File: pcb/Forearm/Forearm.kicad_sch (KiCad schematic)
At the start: 9 parts, among them J1 Conn_01x08_IMU_0, J2 Conn_01x16_Ribbon_To_Top, J3 Conn_01x16_Ribbon_To_Bottom, J4 Conn_01x03_DFR0205, U1 ESP32-S3-DEVKITC-1-N8R2

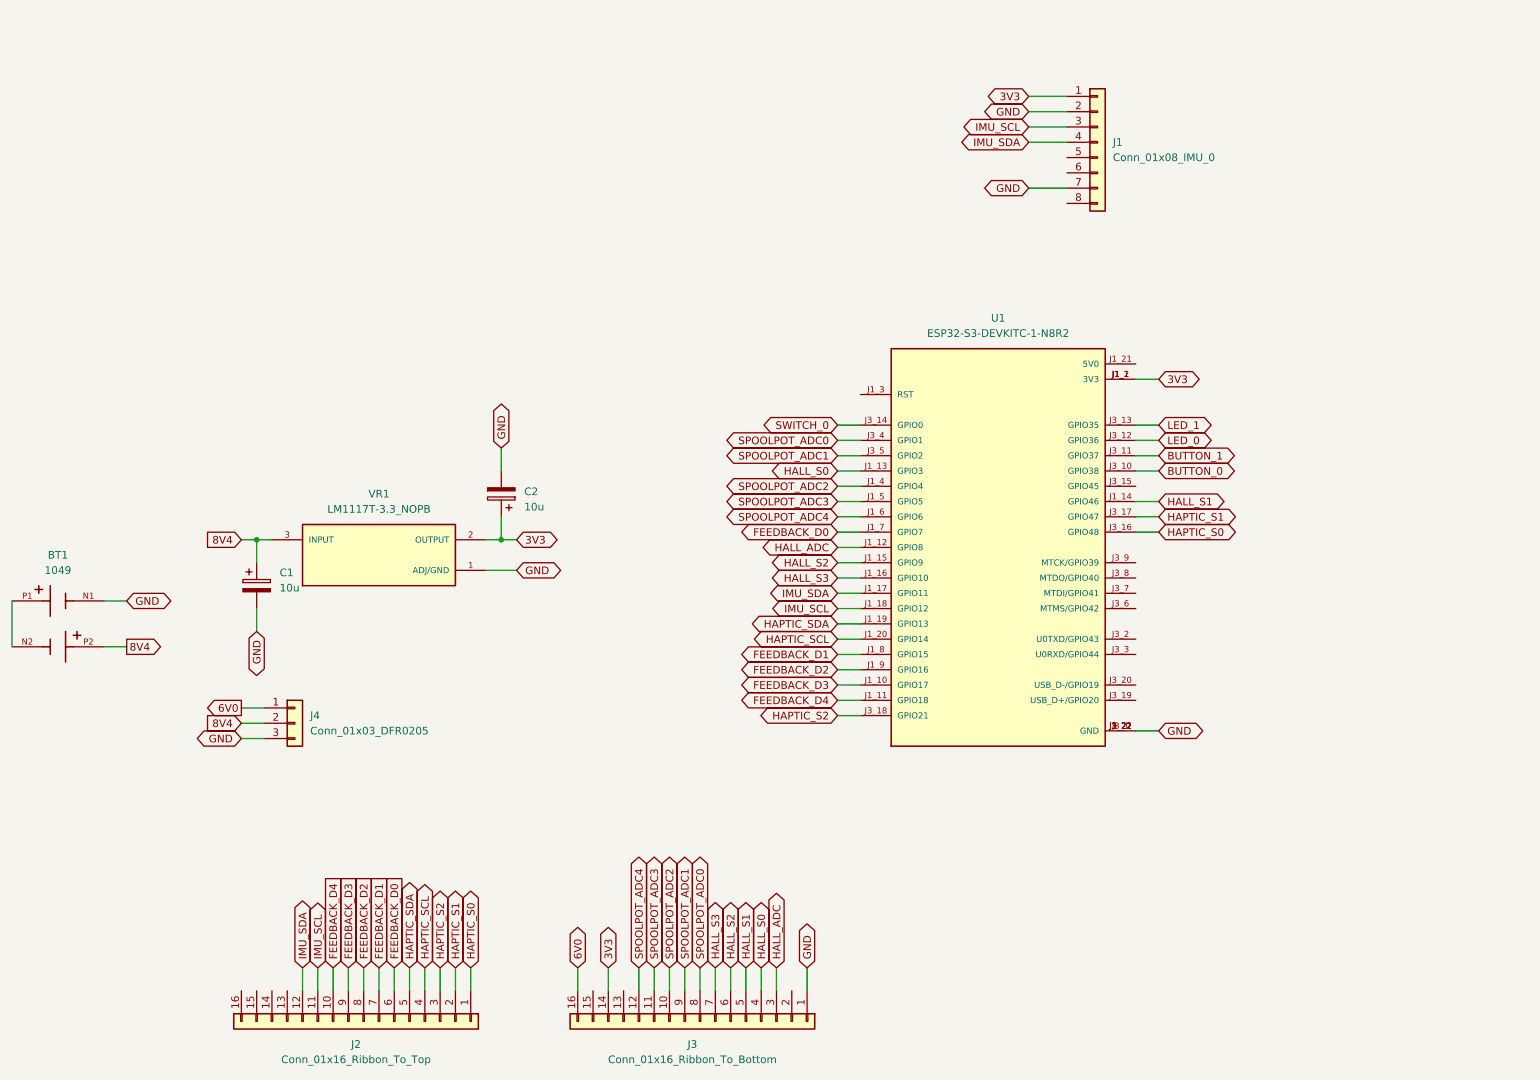
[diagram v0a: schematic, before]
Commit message: merging jackson pcb into main
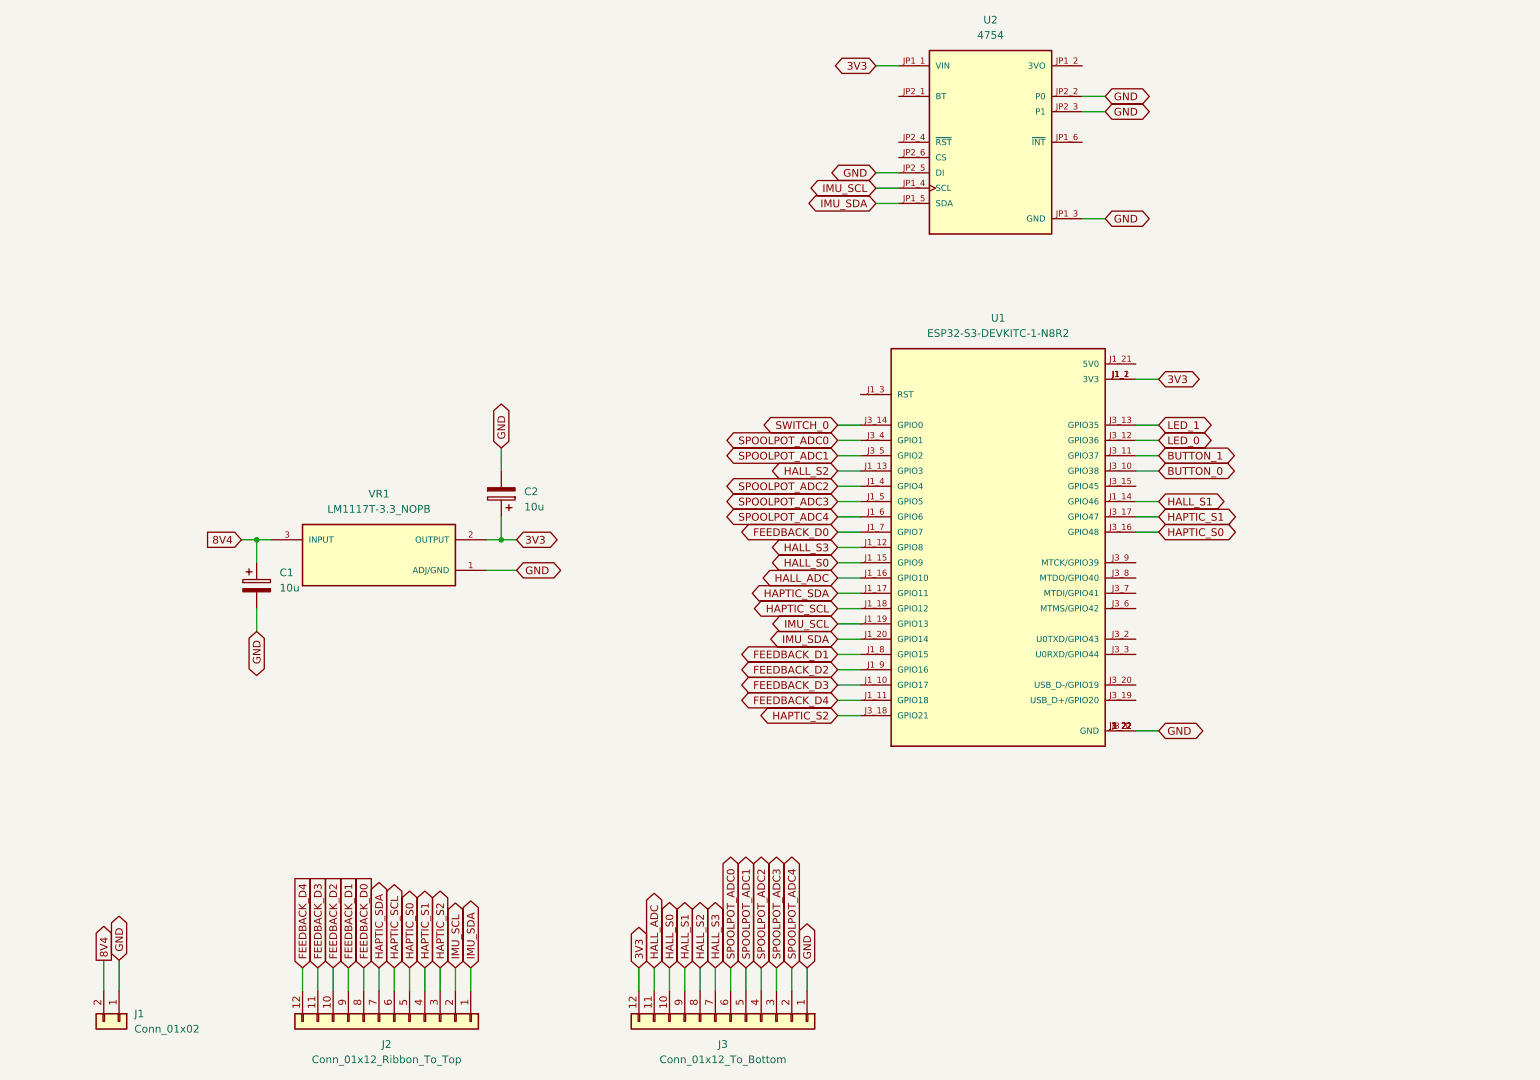
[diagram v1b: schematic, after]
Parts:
- removed BT1: 1049, 1049:BAT_1049, symbol 1049:1049
- removed J1: Conn_01x08_IMU_0, symbol Connector_Generic:Conn_01x08
- removed J2: Conn_01x16_Ribbon_To_Top, symbol Connector_Generic:Conn_01x16
- removed J3: Conn_01x16_Ribbon_To_Bottom, symbol Connector_Generic:Conn_01x16
- removed J4: Conn_01x03_DFR0205, symbol Connector_Generic:Conn_01x03
- added J1: Conn_01x02, Connector_PinSocket_2.54mm:PinSocket_1x02_P2.54mm_Vertical, symbol Connector_Generic:Conn_01x02
- added J2: Conn_01x12_Ribbon_To_Top, 0522071233:0522071233, symbol Connector_Generic:Conn_01x12
- added J3: Conn_01x12_To_Bottom, 0522071233:0522071233, symbol Connector_Generic:Conn_01x12
- added U2: 4754, BNO085:MODULE_4754, symbol BNO085:4754
- C1, C2: footprint (none) -> Capacitor_SMD:C_1206_3216Metric
- VR1: footprint LM1117T-3.3_NOPB:TO254P1054X470X1955-3 -> LM1117T-3.3:LM1117T-3.3_NOPB
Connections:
- net 3V3: now also J3.12 (Pin_12), U2.JP1_1 (VIN)
- net 8V4: now also J1.2 (Pin_2)
- net FEEDBACK_D0: now also J2.8 (Pin_8)
- net FEEDBACK_D1: now also J2.9 (Pin_9)
- net FEEDBACK_D2: now also J2.10 (Pin_10)
- net FEEDBACK_D3: now also J2.11 (Pin_11)
- net FEEDBACK_D4: now also J2.12 (Pin_12)
- net GND: now also J1.1 (Pin_1), J3.1 (Pin_1), U2.JP1_3 (GND), U2.JP2_2 (P0), U2.JP2_3 (P1), U2.JP2_5 (DI)
- net HALL_ADC: now also U1.J1_16 (GPIO10), J3.11 (Pin_11); no longer U1.J1_12 (GPIO8)
- net HALL_S0: now also U1.J1_15 (GPIO9), J3.10 (Pin_10); no longer U1.J1_13 (GPIO3)
- net HALL_S1: now also J3.9 (Pin_9)
- net HALL_S2: now also U1.J1_13 (GPIO3), J3.8 (Pin_8); no longer U1.J1_15 (GPIO9)
- net HALL_S3: now also U1.J1_12 (GPIO8), J3.7 (Pin_7); no longer U1.J1_16 (GPIO10)
- net HAPTIC_S0: now also J2.5 (Pin_5)
- net HAPTIC_S1: now also J2.4 (Pin_4)
- net HAPTIC_S2: now also J2.3 (Pin_3)
- net HAPTIC_SCL: now also U1.J1_18 (GPIO12), J2.6 (Pin_6); no longer U1.J1_20 (GPIO14)
- net HAPTIC_SDA: now also U1.J1_17 (GPIO11), J2.7 (Pin_7); no longer U1.J1_19 (GPIO13)
- net IMU_SCL: now also U1.J1_19 (GPIO13), J2.2 (Pin_2), U2.JP1_4 (SCL); no longer U1.J1_18 (GPIO12)
- net IMU_SDA: now also U1.J1_20 (GPIO14), J2.1 (Pin_1), U2.JP1_5 (SDA); no longer U1.J1_17 (GPIO11)
- net SPOOLPOT_ADC0: now also J3.6 (Pin_6)
- net SPOOLPOT_ADC1: now also J3.5 (Pin_5)
- net SPOOLPOT_ADC2: now also J3.4 (Pin_4)
- net SPOOLPOT_ADC3: now also J3.3 (Pin_3)
- net SPOOLPOT_ADC4: now also J3.2 (Pin_2)

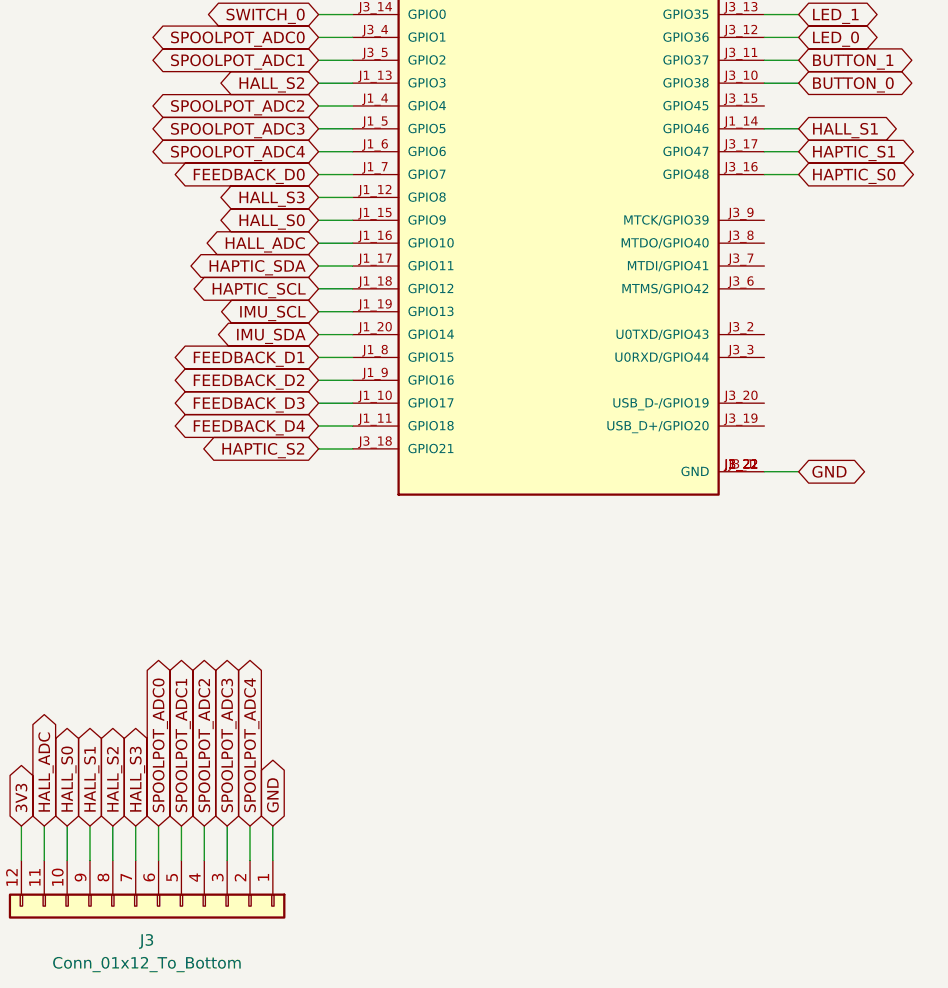
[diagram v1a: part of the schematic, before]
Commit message: re-routed forearm board w/o switches etc
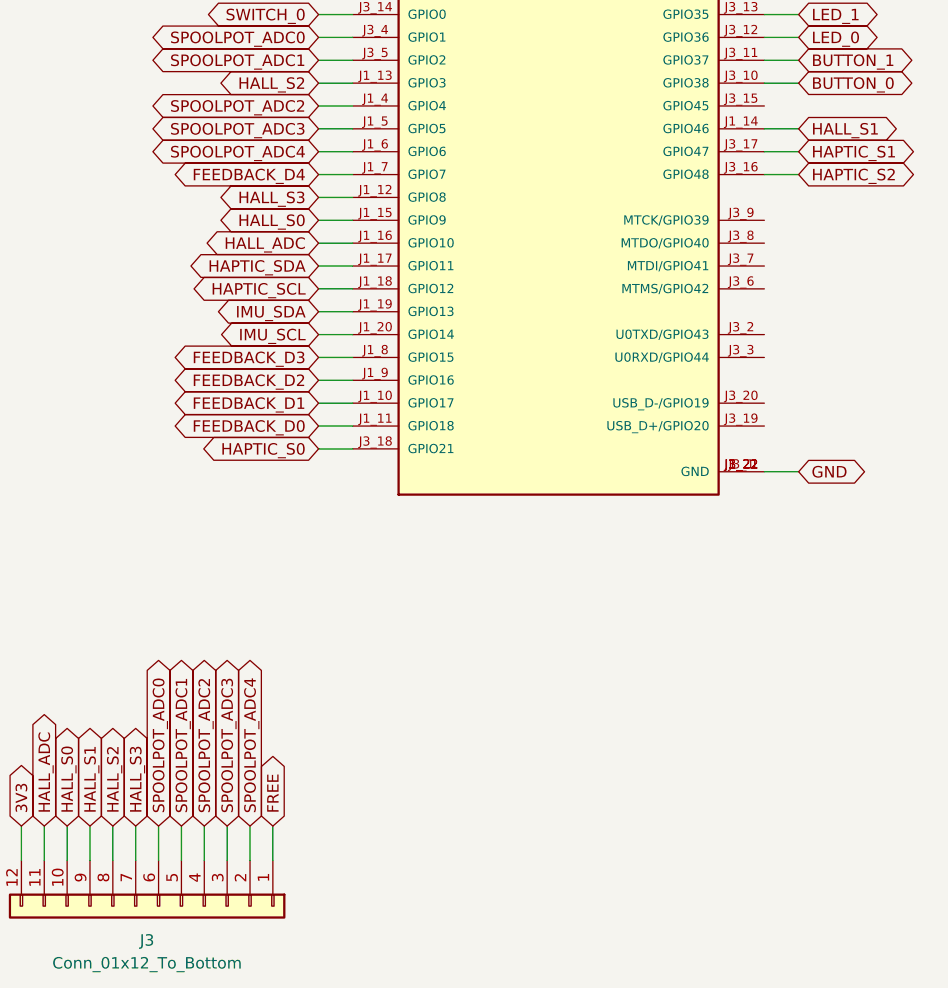
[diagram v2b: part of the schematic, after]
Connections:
- net FEEDBACK_D0: now also U1.J1_11 (GPIO18); no longer U1.J1_7 (GPIO7)
- net FEEDBACK_D1: now also U1.J1_10 (GPIO17); no longer U1.J1_8 (GPIO15)
- net FEEDBACK_D3: now also U1.J1_8 (GPIO15); no longer U1.J1_10 (GPIO17)
- net FEEDBACK_D4: now also U1.J1_7 (GPIO7); no longer U1.J1_11 (GPIO18)
- net GND: no longer J3.1 (Pin_1)
- net HAPTIC_S0: now also U1.J3_18 (GPIO21); no longer U1.J3_16 (GPIO48)
- net HAPTIC_S2: now also U1.J3_16 (GPIO48); no longer U1.J3_18 (GPIO21)
- net IMU_SCL: now also U1.J1_20 (GPIO14); no longer U1.J1_19 (GPIO13)
- net IMU_SDA: now also U1.J1_19 (GPIO13); no longer U1.J1_20 (GPIO14)
- new net FREE: J3.1 (Pin_1)

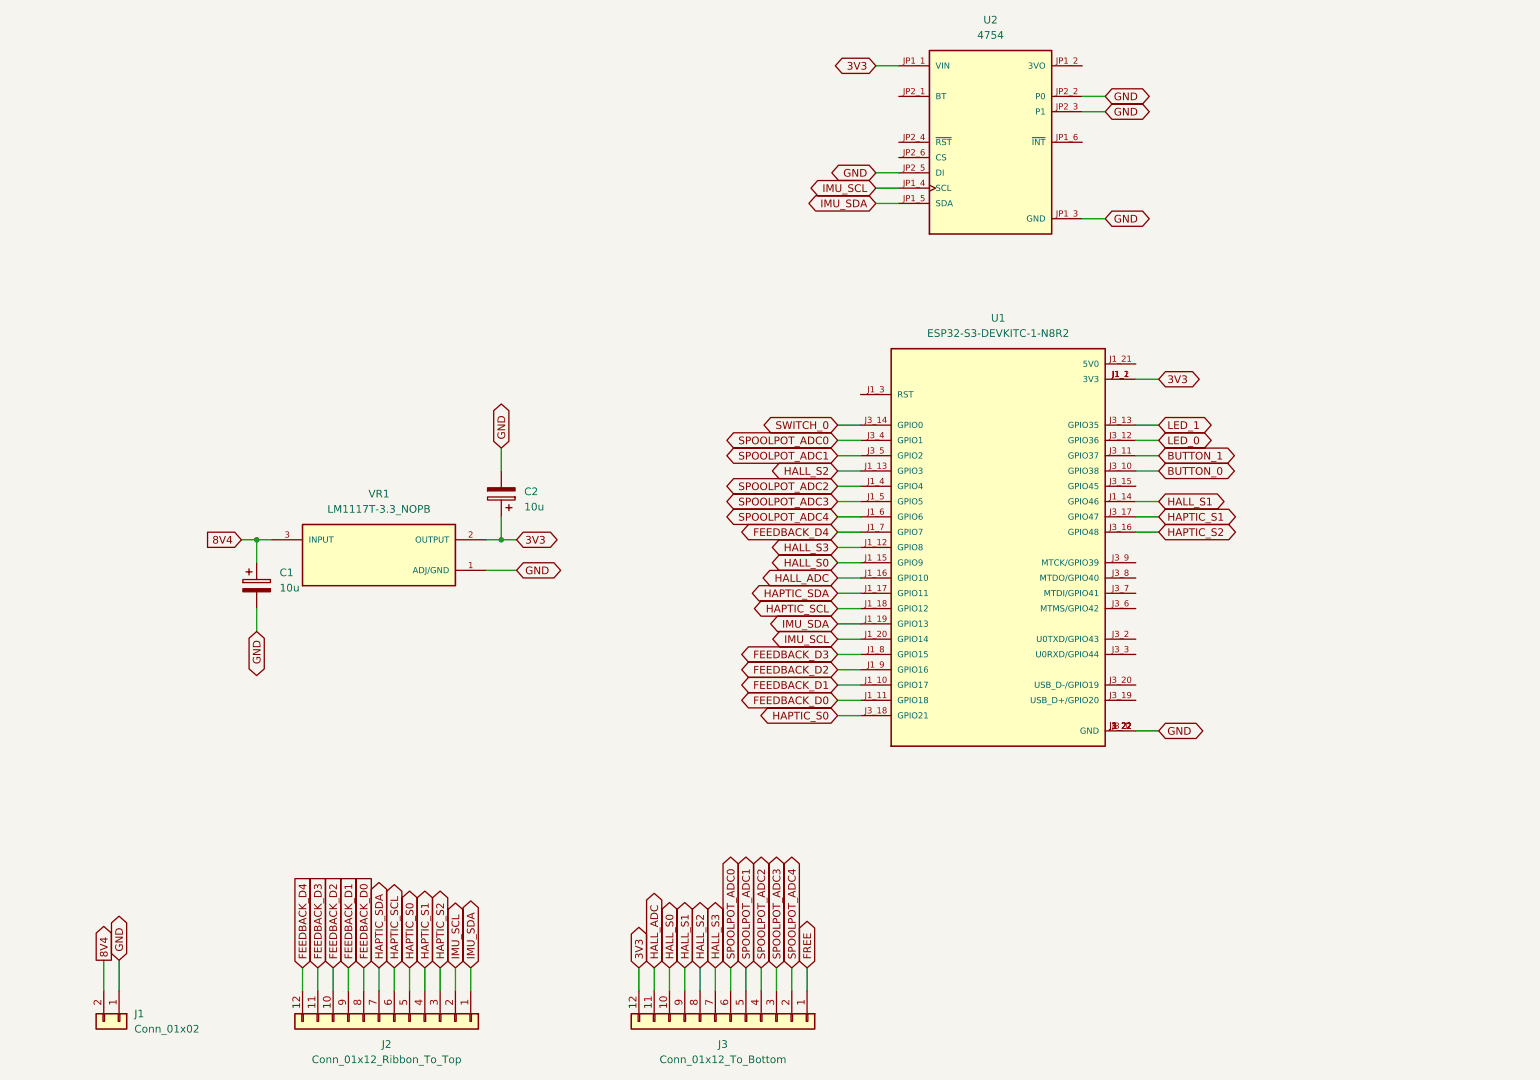
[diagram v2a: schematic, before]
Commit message: revised pcbs in preparation for pcb review; added pull-ups etc to forearm
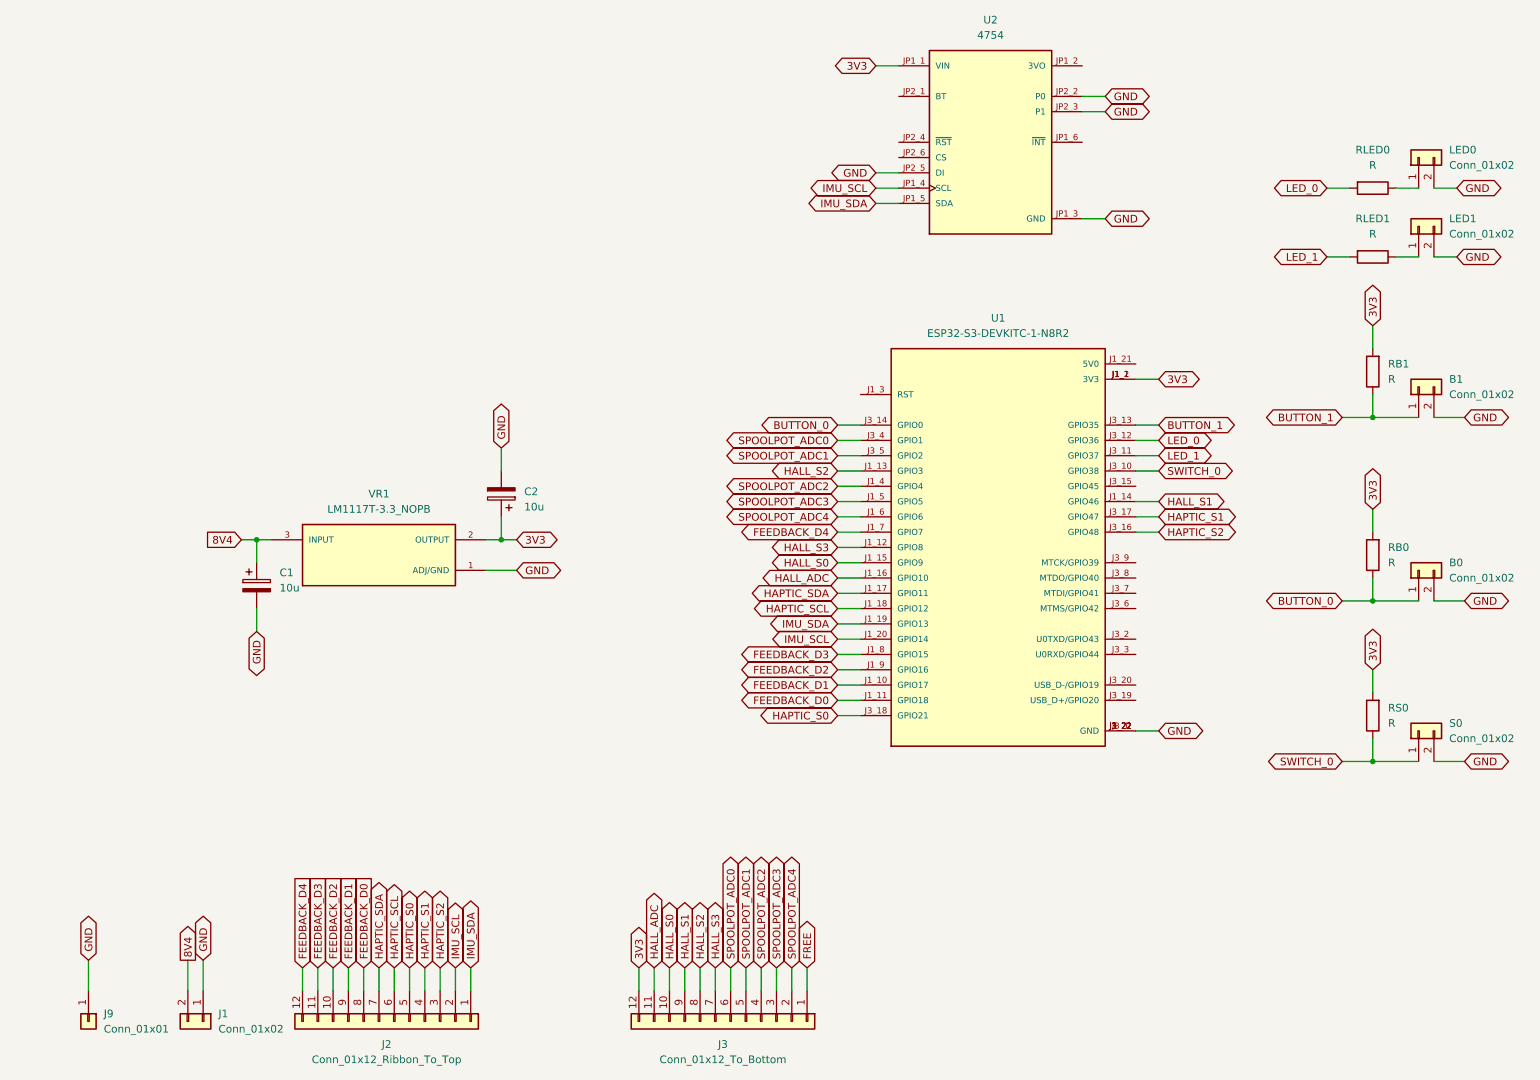
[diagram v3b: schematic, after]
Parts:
- added B0, B1, LED0, LED1, S0: Conn_01x02, Connector_PinSocket_2.54mm:PinSocket_1x02_P2.54mm_Vertical, symbol Connector_Generic:Conn_01x02
- added J9: Conn_01x01, Connector_PinSocket_2.54mm:PinSocket_1x01_P2.54mm_Vertical, symbol Connector_Generic:Conn_01x01
- added RB0, RB1, RLED0, RLED1, RS0: R, Resistor_SMD:R_0402_1005Metric, symbol Device:R
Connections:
- net 3V3: now also RB0.2, RB1.2, RS0.2
- net BUTTON_0: now also U1.J3_14 (GPIO0), B0.1 (Pin_1), RB0.1; no longer U1.J3_10 (GPIO38)
- net BUTTON_1: now also U1.J3_13 (GPIO35), B1.1 (Pin_1), RB1.1; no longer U1.J3_11 (GPIO37)
- net GND: now also B0.2 (Pin_2), B1.2 (Pin_2), J9.1 (Pin_1), LED0.2 (Pin_2), LED1.2 (Pin_2), S0.2 (Pin_2)
- net LED_0: now also RLED0.2
- net LED_1: now also U1.J3_11 (GPIO37), RLED1.2; no longer U1.J3_13 (GPIO35)
- net SWITCH_0: now also U1.J3_10 (GPIO38), RS0.1, S0.1 (Pin_1); no longer U1.J3_14 (GPIO0)
- new net: LED1.1 (Pin_1), RLED1.1
- new net: LED0.1 (Pin_1), RLED0.1
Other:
- moved on the sheet: J1
